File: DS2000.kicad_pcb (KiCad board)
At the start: 4 copper layers, 72 x 46 mm, 60 parts, among them J1 USB-C, J3 USB wire, SW1 MUTE, SW2 DEAFEN, SW3 DISCONNECT, U1 USBLC6-2SC6, U2 XC6206P332MR, U3 RP2350A, U4 W25Q32JVSS, U5 74AHCT1G125, Y1 12MHz

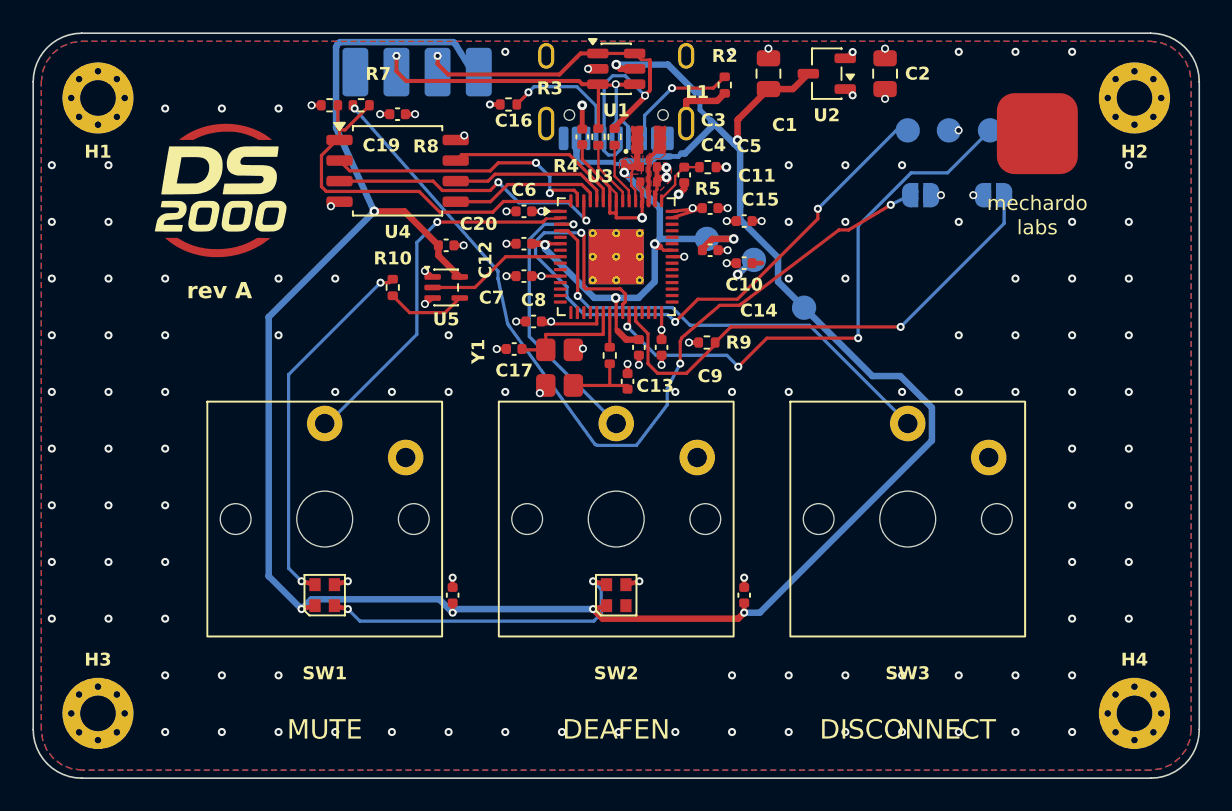
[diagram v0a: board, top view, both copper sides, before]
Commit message: feat: hybrid Choc V1 / MX switch footprint for prototypes
SW1-SW3 take either a Kailh Choc V1 (product) or a 3-pin MX (prototypes):
MX pins added, shared 4 mm centre hole, tracks moved off the new pins.

Co-Authored-By: Claude Opus 5.5 <noreply@anthropic.com>
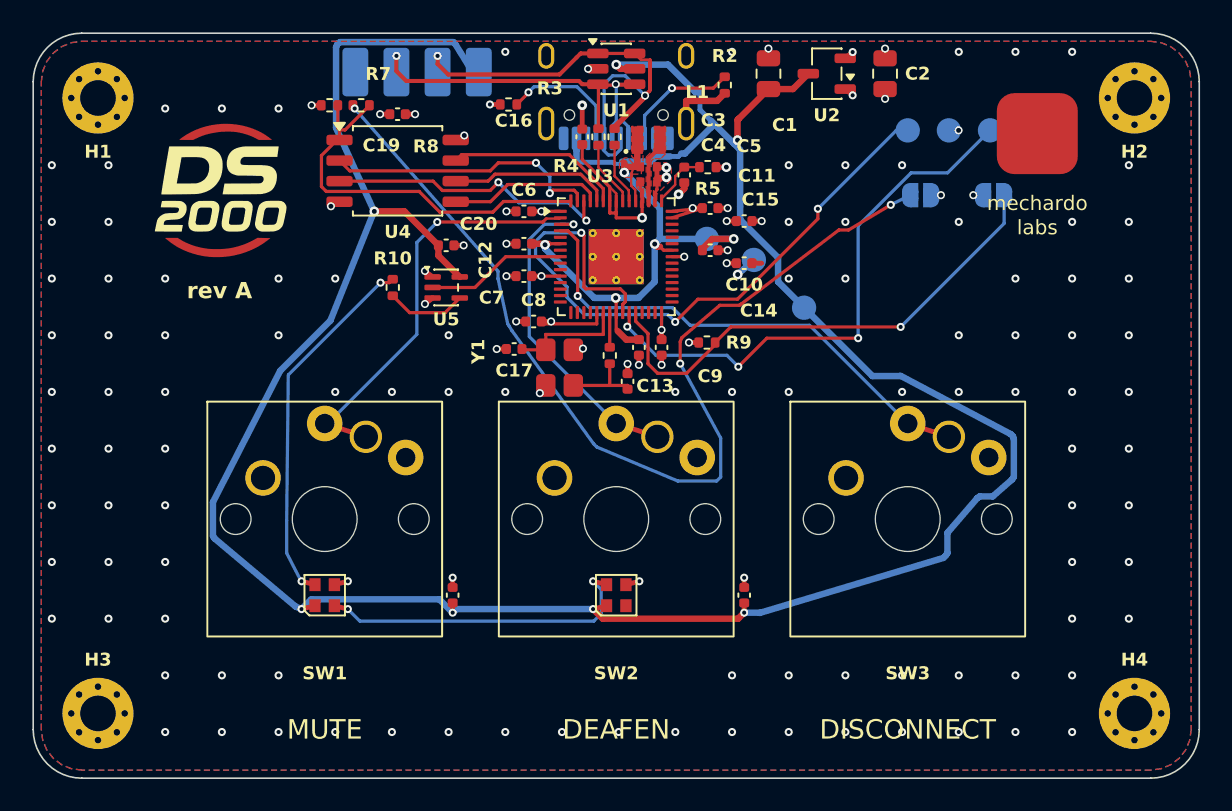
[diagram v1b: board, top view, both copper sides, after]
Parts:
- SW1, SW2, SW3: footprint DS2000:SW_Kailh_Choc_V1_1.00u -> DS2000:SW_Hybrid_Choc_V1_MX_1.00u
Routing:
- net +5V: track 158.7 -> 170.2 mm
- net Net-(JP1-B): track 53.2 -> 60.7 mm
- net Net-(U3-GPIO2): track 28.4 -> 31.0 mm
- net Net-(U3-GPIO1): track 17.5 -> 20.2 mm
- net Net-(U3-GPIO0): track 23.1 -> 25.8 mm

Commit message: fix: redraw the moved switch-area tracks as straight 45-degree runs
Co-Authored-By: Claude Opus 5.5 <noreply@anthropic.com>
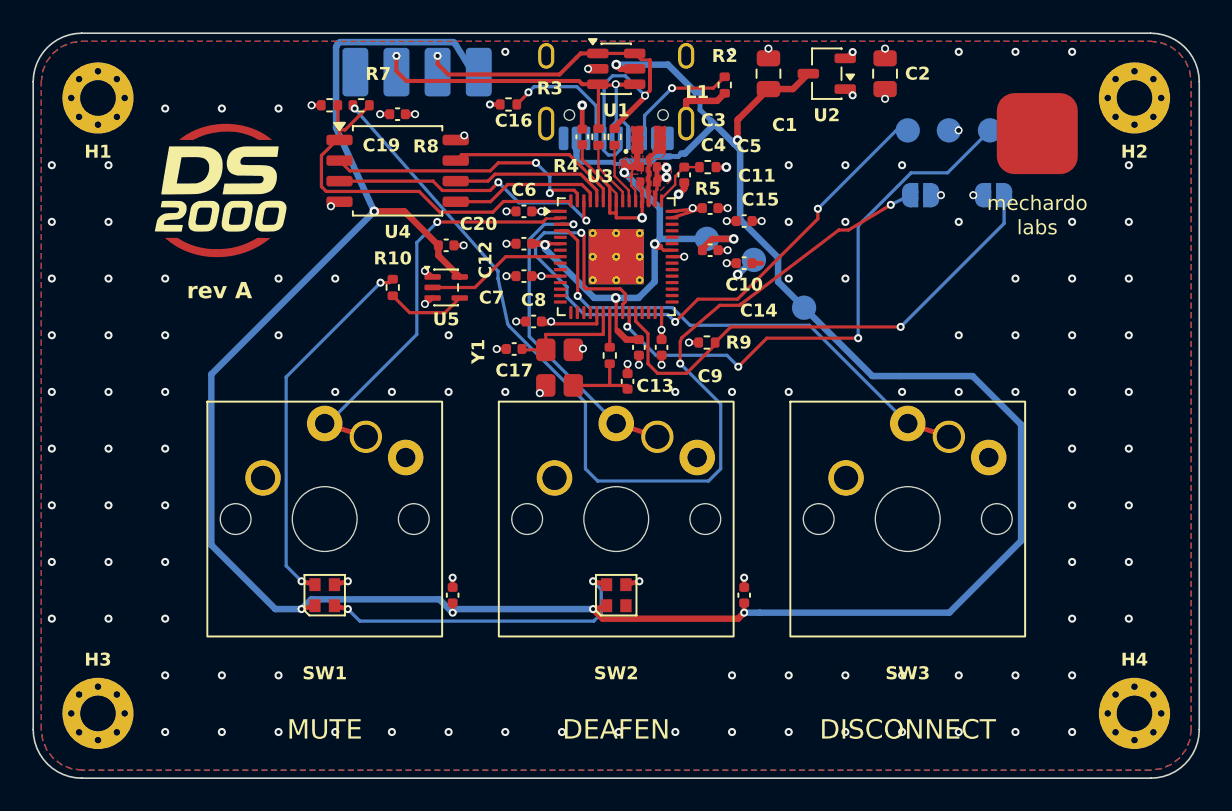
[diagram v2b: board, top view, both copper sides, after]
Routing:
- net +5V: track 170.2 -> 176.6 mm
- net Net-(JP1-B): track 60.7 -> 62.9 mm
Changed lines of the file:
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@@
 	)
 	(segment
-		(start 75.1 102.05)
-		(end 75.2 102.2)
+		(start 125 95.17)
+		(end 125 102.35)
+		(width 0.4)
+		(locked yes)
+		(layer "B.Cu")
+		(net "+5V")
+	)
+	(segment
+		(start 85.062 82.001)
+		(end 75 92.063)
 		(width 0.4)
 		(locked yes)
@@
 	)
 	(segment
-		(start 124.35 95.75)
-		(end 124.5 95.9)
-		(width 0.4)
-		(locked yes)
-		(layer "B.Cu")
-		(net "+5V")
-	)
-	(segment
-		(start 123.25 99.6)
-		(end 122.45 99.6)
+		(start 117.546 92.17)
+		(end 122 92.17)
 		(width 0.4)
 		(locked yes)
@@
 		(start 82.7 76.85)
 		(end 85.05 82)
-		(width 0.4)
-		(locked yes)
-		(layer "B.Cu")
-		(net "+5V")
-	)
-	(segment
-		(start 120.45 103.1)
-		(end 120.35 103.25)
 		(width 0.4)
 		(locked yes)
@@
 	)
 	(segment
+		(start 120.57 106.78)
+		(end 108.865 106.78)
+		(width 0.4)
+		(locked yes)
+		(layer "B.Cu")
+		(net "+5V")
+	)
+	(segment
 		(start 91.5 74)
 		(end 90.05 71.65)
@@
 	)
 	(segment
-		(start 75.2 102.2)
-		(end 80.2 106.4)
-		(width 0.4)
-		(locked yes)
-		(layer "B.Cu")
-		(net "+5V")
-	)
-	(segment
 		(start 104.2471 78.4248)
 		(end 105.8554 76.8165)
@@
 	)
 	(segment
-		(start 75.1 99.95)
-		(end 75.1 102.05)
-		(width 0.4)
-		(locked yes)
-		(layer "B.Cu")
-		(net "+5V")
-	)
-	(segment
-		(start 120.35 103.25)
-		(end 120.2 103.4)
+		(start 75 102.6)
+		(end 78.959 106.559)
 		(width 0.4)
 		(locked yes)
@@
 	)
 	(segment
-		(start 79.25 91.85)
-		(end 75.1 99.95)
-		(width 0.4)
-		(locked yes)
-		(layer "B.Cu")
-		(net "+5V")
-	)
-	(segment
 		(start 115.819 92.1699)
 		(end 109.9922 86.3431)
@@
 	)
 	(segment
-		(start 124.45 98.55)
-		(end 123.25 99.6)
-		(width 0.4)
-		(locked yes)
-		(layer "B.Cu")
-		(net "+5V")
-	)
-	(segment
-		(start 124.55 98.4)
-		(end 124.45 98.55)
+		(start 75 92.063)
+		(end 75 102.6)
 		(width 0.4)
 		(locked yes)
@@
 		(end 103.1949 72.9401)
 		(width 0.4)
+		(layer "B.Cu")
+		(net "+5V")
+	)
+	(segment
+		(start 125 102.35)
+		(end 120.57 106.78)
+		(width 0.4)
+		(locked yes)
 		(layer "B.Cu")
 		(net "+5V")
@@
 	)
 	(segment
+		(start 122 92.17)
+		(end 125 95.17)
+		(width 0.4)
+		(locked yes)
+		(layer "B.Cu")
+		(net "+5V")
+	)
+	(segment
 		(start 99.8242 78.969)
 		(end 99.925 79.0698)
@@
 	)
 	(segment
-		(start 117.55 92.15)
-		(end 124.35 95.75)
-		(width 0.4)
-		(locked yes)
-		(layer "B.Cu")
-		(net "+5V")
-	)
-	(segment
-		(start 85.05 82)
-		(end 82.35 88.75)
-		(width 0.4)
-		(locked yes)
-		(layer "B.Cu")
-		(net "+5V")
-	)
-	(segment
 		(start 97.55 78.219)
 		(end 97.55 78.969)
@@
 		(start 82.8 71.65)
 		(end 82.7 71.85)
-		(width 0.4)
-		(locked yes)
-		(layer "B.Cu")
-		(net "+5V")
-	)
-	(segment
-		(start 122.45 99.6)
-		(end 122.3 99.7)
-		(width 0.4)
-		(locked yes)
-		(layer "B.Cu")
-		(net "+5V")
-	)
-	(segment
-		(start 124.55 96.05)
-		(end 124.55 98.4)
 		(width 0.4)
 		(locked yes)
@@
 	)
 	(segment
-		(start 82.35 88.75)
-		(end 79.25 91.85)
-		(width 0.4)
-		(locked yes)
-		(layer "B.Cu")
-		(net "+5V")
-	)
-	(segment
 		(start 82.7 71.85)
 		(end 82.7 76.85)
@@
 	)
 	(segment
-		(start 80.2 106.4)
-		(end 80.55 106.55)
-		(width 0.4)
-		(locked yes)
-		(layer "B.Cu")
-		(net "+5V")
-	)
-	(segment
 		(start 104.0166 78.4248)
 		(end 104.2471 78.4248)
@@
 	)
 	(segment
-		(start 120.2 103.4)
-		(end 108.85 106.8)
-		(width 0.4)
-		(locked yes)
-		(layer "B.Cu")
-		(net "+5V")
-	)
-	(segment
 		(start 89.0773 105.9573)
 		(end 89.9 106.78)
 		(width 0.4)
-		(layer "B.Cu")
-		(net "+5V")
-	)
-	(segment
-		(start 124.5 95.9)
-		(end 124.55 96.05)
-		(width 0.4)
-		(locked yes)
 		(layer "B.Cu")
 		(net "+5V")
@@
 	)
 	(segment
-		(start 120.45 101.85)
-		(end 120.45 103.1)
-		(width 0.4)
-		(locked yes)
-		(layer "B.Cu")
-		(net "+5V")
-	)
-	(segment
-		(start 122.3 99.7)
-		(end 120.45 101.85)
-		(width 0.4)
-		(locked yes)
-		(layer "B.Cu")
-		(net "+5V")
-	)
-	(segment
 		(start 90.121 106.559)
 		(end 89.9 106.78)
@@
 	)
 	(segment
+		(start 78.959 106.559)
+		(end 80.571 106.559)
+		(width 0.4)
+		(locked yes)
+		(layer "B.Cu")
+		(net "+5V")
+	)
+	(segment
 		(start 82.95 71.55)
 		(end 82.8 71.65)
@@
 	)
 	(segment
-		(start 79.75 92.1)
-		(end 79.65 101.1)
+		(start 79.62 103.89)
+		(end 80.571 104.841)
 		(width 0.2)
 		(locked yes)
@@
 	)
 	(segment
-		(start 79.65 103.1)
-		(end 80.55 104.85)
+		(start 85.446 86.404)
+		(end 79.62 92.23)
 		(width 0.2)
 		(locked yes)
@@
 	)
 	(segment
-		(start 79.772 92.0774)
-		(end 85.4458 86.4036)
-		(width 0.2)
-		(layer "B.Cu")
-		(net "Net-(D1-DIN)")
-	)
-	(segment
-		(start 79.65 101.1)
-		(end 79.65 103.1)
+		(start 79.62 92.23)
+		(end 79.62 103.89)
 		(width 0.2)
 		(locked yes)
@@
 	)
 	(segment
-		(start 98.6 96.35)
-		(end 98.8 96.55)
-		(width 0.2)
-		(locked yes)
-		(layer "B.Cu")
-		(net "Net-(JP1-B)")
-	)
-	(segment
-		(start 106.45 96)
-		(end 103.95 91.4)
-		(width 0.2)
-		(locked yes)
-		(layer "B.Cu")
-		(net "Net-(JP1-B)")
-	)
-	(segment
-		(start 93.55 89.35)
-		(end 98.6 96.35)
+		(start 105.7 98.65)
+		(end 106.45 97.9)
 		(width 0.2)
 		(locked yes)
@@
 	)
 	(segment
+		(start 98.1 93.8)
+		(end 98.1 97.9)
+		(width 0.2)
+		(locked yes)
+		(layer "B.Cu")
+		(net "Net-(JP1-B)")
+	)
+	(segment
+		(start 106.45 97.9)
+		(end 106.45 93.9)
+		(width 0.2)
+		(locked yes)
+		(layer "B.Cu")
+		(net "Net-(JP1-B)")
+	)
+	(segment
+		(start 98.85 98.65)
+		(end 105.7 98.65)
+		(width 0.2)
+		(locked yes)
+		(layer "B.Cu")
+		(net "Net-(JP1-B)")
+	)
+	(segment
 		(start 93.4 89.1)
-		(end 93.55 89.35)
-		(width 0.2)
-		(locked yes)
-		(layer "B.Cu")
-		(net "Net-(JP1-B)")
-	)
-	(segment
-		(start 106.45 98.4)
-		(end 106.45 96)
-		(width 0.2)
-		(locked yes)
-		(layer "B.Cu")
-		(net "Net-(JP1-B)")
-	)
-	(segment
-		(start 98.8 96.55)
-		(end 103.8 98.65)
-		(width 0.2)
-		(locked yes)
-		(layer "B.Cu")
-		(net "Net-(JP1-B)")
-	)
-	(segment
-		(start 106.2 98.65)
-		(end 106.45 98.4)
+		(end 98.1 93.8)
 		(width 0.2)
 		(locked yes)
@@
 	)
 	(segment
-		(start 103.8 98.65)
-		(end 106.2 98.65)
+		(start 98.1 97.9)
+		(end 98.85 98.65)
 		(width 0.2)
 		(locked yes)
@@
 		(width 0.2)
 		(locked yes)
+		(layer "B.Cu")
+		(net "Net-(JP1-B)")
+	)
+	(segment
+		(start 106.45 93.9)
+		(end 103.95 91.4)
+		(width 0.2)
+		(locked yes)

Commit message: fix: redraw the long runs as straight lines and 45-degree corners
- +5V: J3 pin 1 drops into one 45-degree line that continues as the
  left side of the ring; under the LEDs the ring is one straight bus on
  B.Cu, and the +5V run that crossed the face under SW2 moves to the back.
- LED row: DIN, DOUT and GND vias level with their pads; D1 -> D2 data
  runs straight beside the bus.
- BOOTSEL: 63 -> 55 mm, no odd angles, beside SWDIO into JP1.
- MX pin 1 -> Choc pin 1: a 45 and a straight run instead of 18 degrees.

DRC unchanged (0 errors, 0 unconnected); every new segment was checked
for 0.2 mm clearance before it was written.

Co-Authored-By: Claude Opus 5.5 <noreply@anthropic.com>
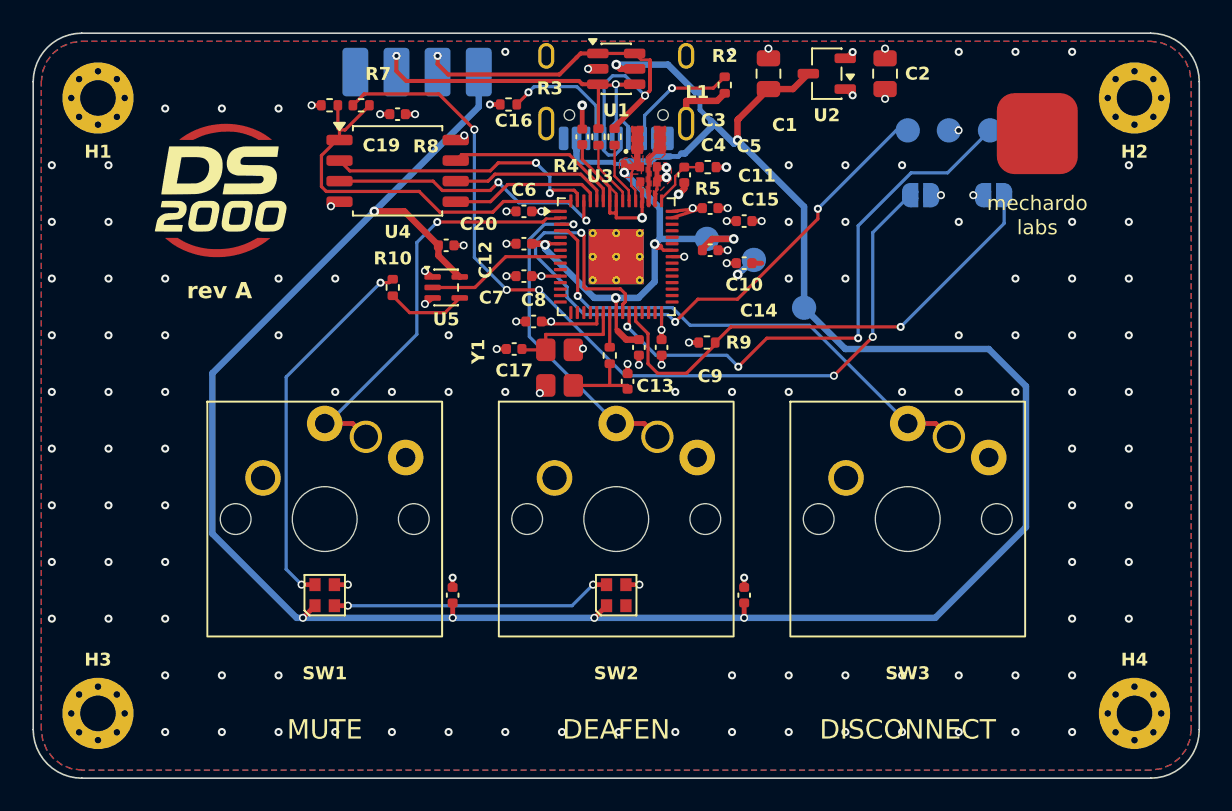
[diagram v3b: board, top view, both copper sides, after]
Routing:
- net +5V: track 176.6 -> 168.3 mm
- net Net-(JP1-B): track 62.9 -> 54.9 mm, vias 3 -> 5
- net Net-(D1-DOUT): track 20.1 -> 17.3 mm

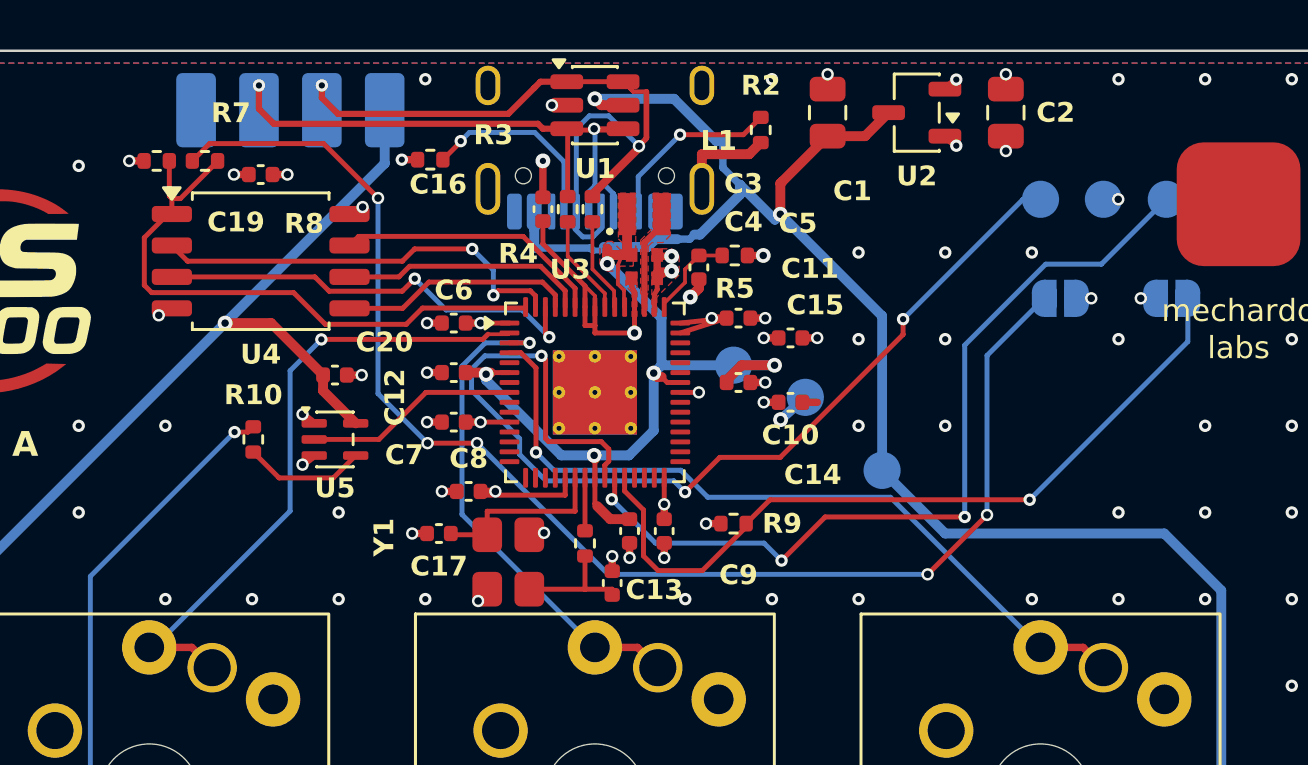
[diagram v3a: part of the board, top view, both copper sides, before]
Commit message: fix: take the vias out of the SMD pads
Fifteen vias overlapped the pad they served: Y1, U1, U2, U4, U5, C1,
C2, JP1, JP2 and TP2. On the reflowed parts the open via would wick
solder from the joint. Each is now a dogbone: a straight or 45-degree
stub from the pad centre to a via 0.12 mm clear of the pad.

To make room, BOOTSEL's first via and vertical move 0.76 mm right, and
R10 -> U5 pin 4 drops 0.35 mm.

J3's two USB vias stay in their wire pads: those are hand-soldered,
and moving the vias would lengthen the USB pair.

DRC unchanged (0 errors, 0 unconnected).

Co-Authored-By: Claude Opus 5.5 <noreply@anthropic.com>
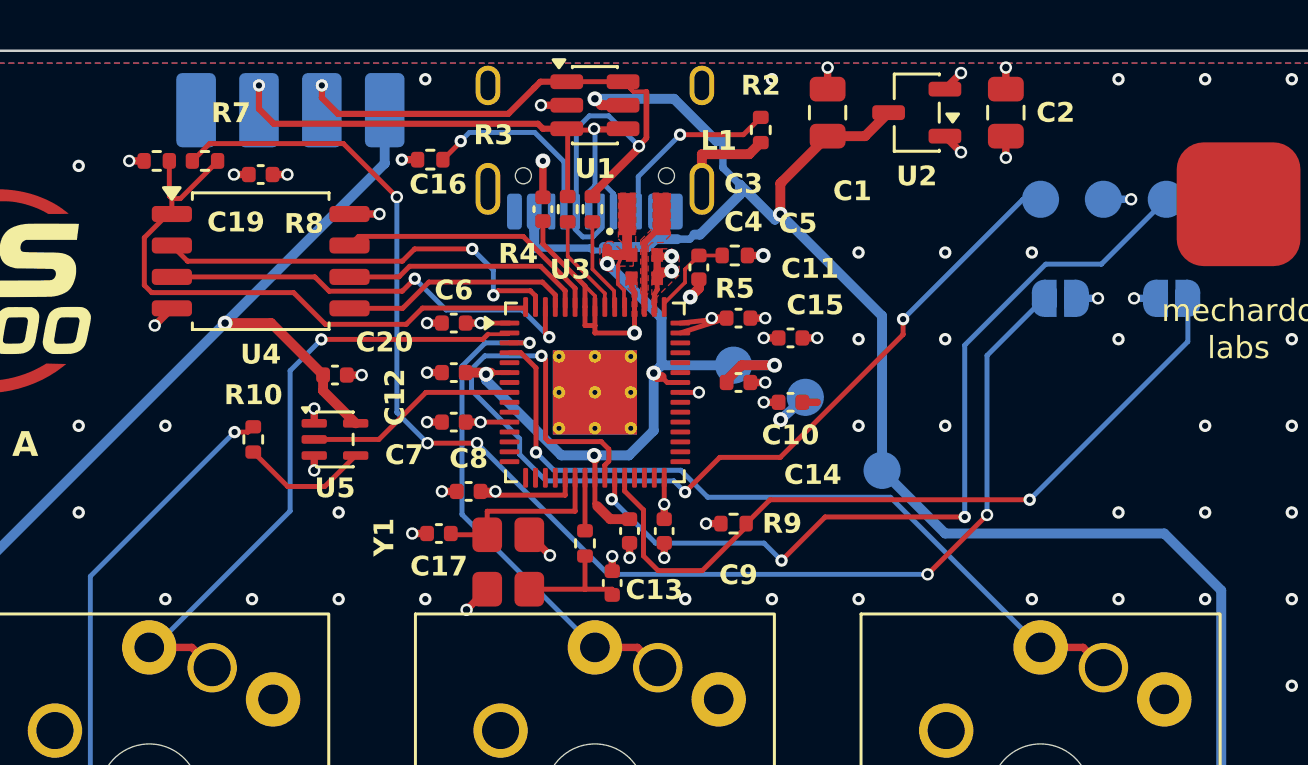
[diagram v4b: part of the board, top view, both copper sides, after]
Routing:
- net GND: track 29.9 -> 33.8 mm
- net +3V3: track 35.1 -> 36.3 mm
